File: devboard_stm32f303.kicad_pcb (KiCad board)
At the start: 2 copper layers, 50 x 17.8 mm, 22 parts, among them J1 Conn_01x04, J2 USB_B_Mini, J3 Conn_01x20, J4 Conn_01x20, SW1 SW_Push, U1 STM32F303CCTx, U2 AMS1117-3.3, Y1 Crystal_Small

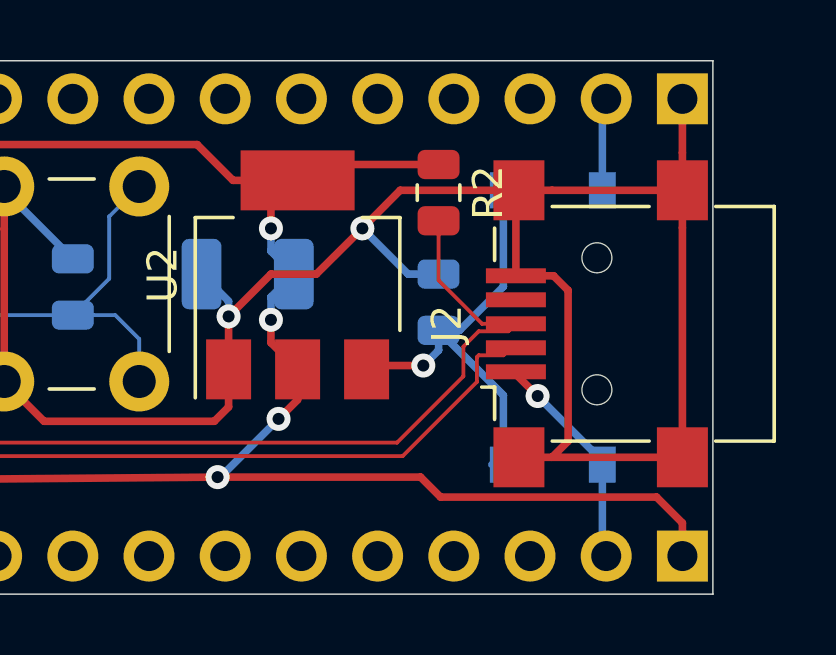
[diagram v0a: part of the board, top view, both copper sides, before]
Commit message: Add netlist tags
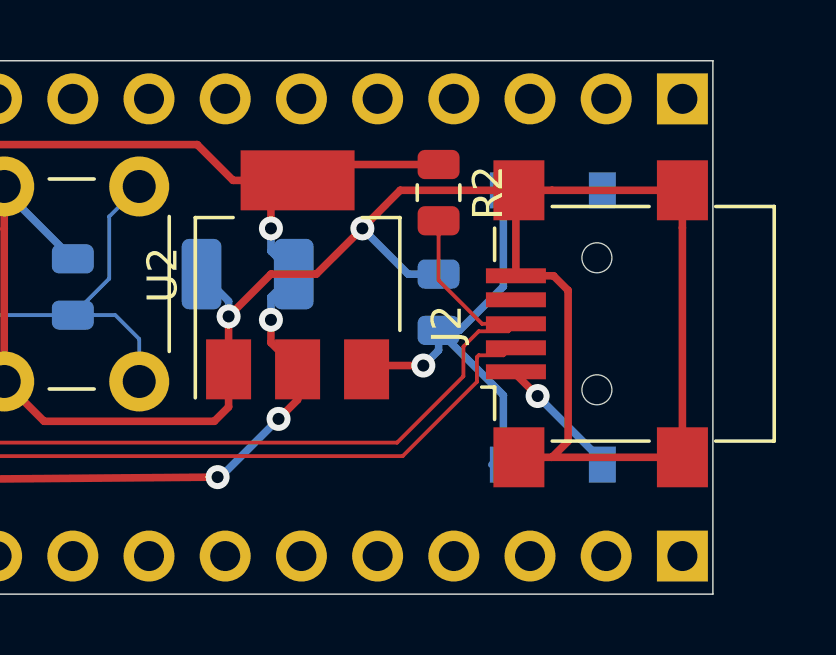
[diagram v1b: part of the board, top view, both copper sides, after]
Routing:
- net +3V3: track 125.7 -> 108.5 mm
- net GND: track 131.6 -> 128.6 mm
- net VBUS: track 7.39 -> 4.47 mm
- net VIN: track 2.85 -> 0.18 mm
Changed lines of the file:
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@@
     (thickness 1.6)
     (drawings 9)
-    (tracks 238)
+    (tracks 229)
     (zones 0)
     (modules 22)
@@
   (segment (start 125.589 30.875) (end 125.589 32.639) (width 0.254) (layer F.Cu) (net 1))
   (segment (start 127 29.464) (end 125.589 30.875) (width 0.254) (layer F.Cu) (net 1))
-  (segment (start 140.716 25.416) (end 140.716 23.622) (width 0.254) (layer F.Cu) (net 1))
-  (segment (start 140.716 26.67) (end 140.716 25.416) (width 0.254) (layer F.Cu) (net 1))
   (via (at 130.048 27.94) (size 0.8) (drill 0.4) (layers F.Cu B.Cu) (net 1))
   (segment (start 131.572 29.464) (end 130.048 27.94) (width 0.254) (layer B.Cu) (net 1))
@@
   (segment (start 101.91752 36.91402) (end 113.70798 36.91402) (width 0.254) (layer F.Cu) (net 4))
   (segment (start 128.016 26.466) (end 127.889 26.339) (width 0.254) (layer F.Cu) (net 4))
-  (segment (start 139.855001 36.897001) (end 132.655001 36.897001) (width 0.254) (layer F.Cu) (net 4))
-  (segment (start 140.716 37.758) (end 139.855001 36.897001) (width 0.254) (layer F.Cu) (net 4))
-  (segment (start 140.716 38.862) (end 140.716 37.758) (width 0.254) (layer F.Cu) (net 4))
-  (segment (start 131.989 36.231) (end 132.655001 36.897001) (width 0.254) (layer F.Cu) (net 4))
-  (segment (start 125.222 36.231) (end 131.989 36.231) (width 0.254) (layer F.Cu) (net 4))
   (segment (start 127.889 32.639) (end 127.889 31.877) (width 0.254) (layer F.Cu) (net 4))
   (segment (start 127.889 26.339) (end 127.889 27.051) (width 0.254) (layer F.Cu) (net 4))
@@
   (segment (start 103.886 28.448) (end 104.902 29.464) (width 0.127) (layer B.Cu) (net 12))
   (segment (start 138.048 23.75) (end 138.176 23.622) (width 0.254) (layer B.Cu) (net 81))
-  (segment (start 138.048 26.416) (end 138.048 23.75) (width 0.254) (layer B.Cu) (net 81))
   (segment (start 138.048 38.734) (end 138.176 38.862) (width 0.254) (layer B.Cu) (net 82))
-  (segment (start 138.048 35.814) (end 138.048 38.734) (width 0.254) (layer B.Cu) (net 82))
   (via (at 135.89 33.528) (size 0.8) (drill 0.4) (layers F.Cu B.Cu) (net 82))
   (segment (start 135.166 32.72) (end 135.166 32.804) (width 0.254) (layer F.Cu) (net 82))

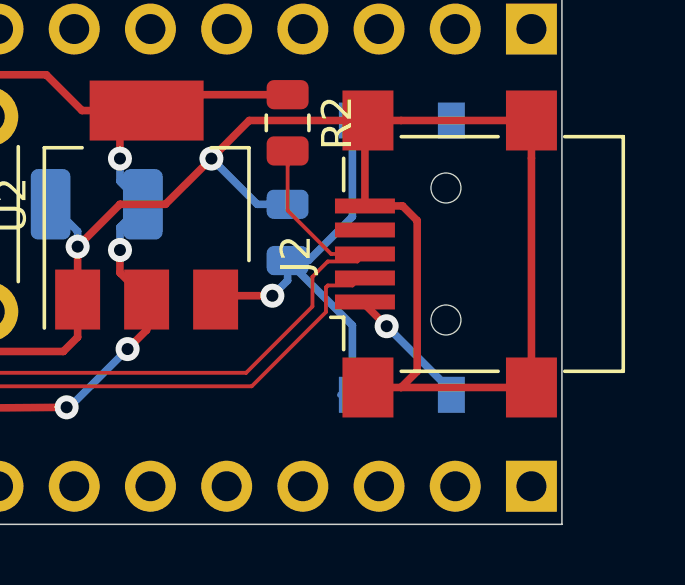
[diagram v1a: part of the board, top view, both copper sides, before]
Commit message: Add polyfuse
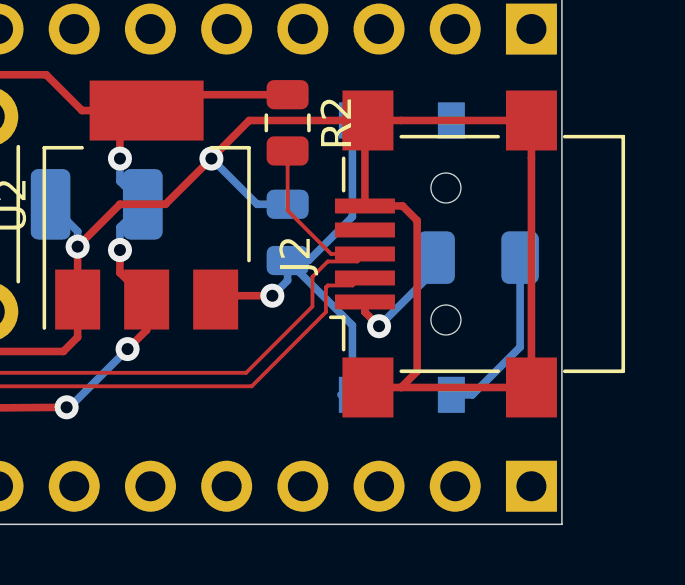
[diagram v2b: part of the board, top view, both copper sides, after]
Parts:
- added F1: Polyfuse_Small, Fuse:Fuse_1206_3216Metric, B.Cu at (138.9, 31.2)
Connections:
- net BOOT1 renamed PB2
- net Net-(U1-Pad10) renamed PA0
- net Net-(U1-Pad11) renamed PA1
- net Net-(U1-Pad12) renamed PA2
- net Net-(U1-Pad13) renamed PA3
- net Net-(U1-Pad14) renamed PA4
- net Net-(U1-Pad15) renamed PA5
- net Net-(U1-Pad16) renamed PA6
- net Net-(U1-Pad17) renamed PA7
- net Net-(U1-Pad18) renamed PB0
- net Net-(U1-Pad19) renamed PB1
- net Net-(U1-Pad21) renamed PB10
- net Net-(U1-Pad22) renamed PB11
- net Net-(U1-Pad25) renamed PB12
- net Net-(U1-Pad26) renamed PB13
- net Net-(U1-Pad27) renamed PB14
- net Net-(U1-Pad28) renamed PB15
- net Net-(U1-Pad29) renamed PA8
- net Net-(U1-Pad30) renamed PA9
- net Net-(U1-Pad31) renamed PA10
- net Net-(U1-Pad39) renamed PB3
- net Net-(U1-Pad40) renamed PB4
- net Net-(U1-Pad41) renamed PB5
- net Net-(U1-Pad42) renamed PB6
- net Net-(U1-Pad43) renamed PB7
- net Net-(U1-Pad45) renamed PB8
- net Net-(U1-Pad46) renamed PB9
- J2 pad 1: VBUS -> Net-(F1-Pad1)
- J3 pad 1: GND -> Net-(J3-Pad1)
- J3 pad 2: VIN -> Net-(J3-Pad2)
- J4 pad 1: +3V3 -> VBUS
- J4 pad 2: VBUS -> GND
- J4 pad 3: Net-(J4-Pad3) -> RESET
- J4 pad 4: Net-(J4-Pad4) -> +3V3
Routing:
- net Net-(F1-Pad1): track 0.00 -> 4.16 mm, vias 0 -> 1
- net VBUS: track 4.47 -> 6.06 mm, vias 1 -> 0

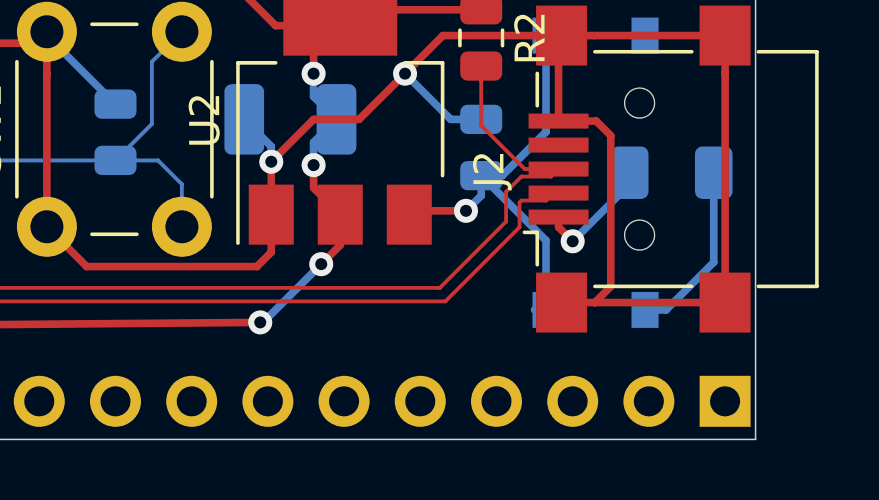
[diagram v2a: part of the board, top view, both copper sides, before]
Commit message: Power routing
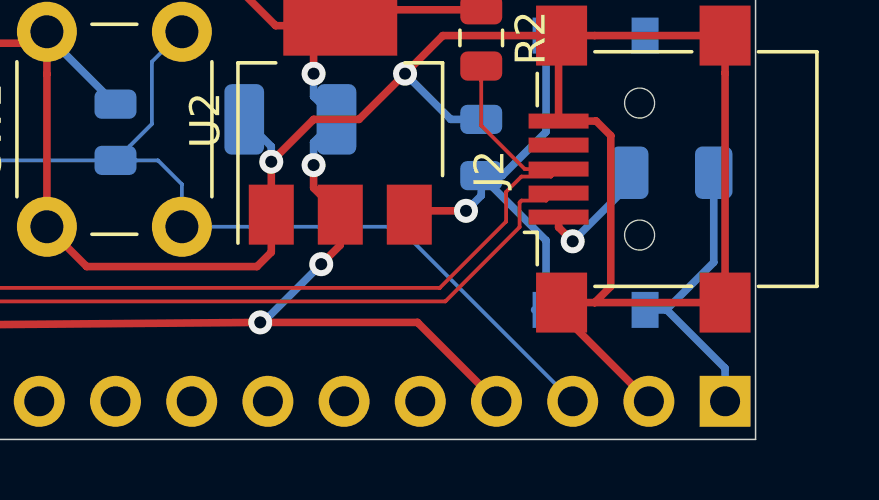
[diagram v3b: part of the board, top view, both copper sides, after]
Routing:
- net RESET: track 29.3 -> 44.8 mm
- net +3V3: track 108.5 -> 117.4 mm
- net GND: track 128.8 -> 133.3 mm
- net VBUS: track 6.06 -> 9.93 mm

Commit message: Start new routing
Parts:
- removed J1: Conn_01x04, Connector_PinHeader_2.54mm:PinHeader_1x04_P2.54mm_Vertical
- removed SW1: SW_Push, Button_Switch_THT:SW_PUSH_6mm
- C5: moved to B.Cu
- D1: moved to F.Cu
- JP1: footprint Connector_PinHeader_2.54mm:PinHeader_1x03_P2.54mm_Vertical -> Jumper:SolderJumper-3_P1.3mm_Open_Pad1.0x1.5mm
- moved JP1 30.3 mm to (84.6, 30.2), turned to 90 degrees
- moved R1 30.0 mm to (81.6, 30.5)
- moved C1 20.5 mm to (115.6, 33.4), turned to 90 degrees
- moved C2 20.2 mm to (115.6, 29.8), turned to 270 degrees
- moved Y1 16.4 mm to (112.6, 31.6), turned to 90 degrees
- moved D2 15.0 mm to (149.7, 33.5)
- moved C8 10.3 mm to (142.7, 31.9)
- moved F1 6.61 mm to (132.3, 31.1), turned to 270 degrees
- moved C6 5.42 mm to (120.1, 35.3), turned to 0 degrees
- moved D1 4.98 mm to (131.4, 35.3)
- moved C5 1.31 mm to (111.4, 36.1), turned to 180 degrees
- moved C3 1.25 mm to (111.4, 26.4)
- moved C7 1.15 mm to (98.5, 26.4), turned to 0 degrees
- moved C4 1.14 mm to (98.5, 36.1)
- moved U2 0.38 mm to (127.5, 29.5)
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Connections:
- net Net-(J3-Pad18) renamed PA15
- J3 pad 1: Net-(J3-Pad1) -> PA9
- J3 pad 10: Net-(J3-Pad10) -> PB2
- J3 pad 11: Net-(J3-Pad11) -> PB1
- J3 pad 12: Net-(J3-Pad12) -> PB0
- J3 pad 13: Net-(J3-Pad13) -> PA4
- J3 pad 14: Net-(J3-Pad14) -> PA5
- J3 pad 15: Net-(J3-Pad15) -> PA6
- J3 pad 16: Net-(J3-Pad16) -> PA7
- J3 pad 17: Net-(J3-Pad17) -> PA8
- J3 pad 2: Net-(J3-Pad2) -> PA10
- J3 pad 3: Net-(J3-Pad3) -> GND
- J3 pad 4: Net-(J3-Pad4) -> GND
- J3 pad 5: Net-(J3-Pad5) -> PB7
- J3 pad 6: Net-(J3-Pad6) -> PB6
- J3 pad 7: Net-(J3-Pad7) -> PB5
- J3 pad 8: Net-(J3-Pad8) -> PB4
- J3 pad 9: Net-(J3-Pad9) -> PB3
- J4 pad 10: Net-(J4-Pad10) -> PB14
- J4 pad 11: Net-(J4-Pad11) -> PB15
- J4 pad 12: Net-(J4-Pad12) -> PB9
- J4 pad 13: Net-(J4-Pad13) -> PB10
- J4 pad 14: Net-(J4-Pad14) -> PB11
- J4 pad 15: Net-(J4-Pad15) -> PB12
- J4 pad 16: Net-(J4-Pad16) -> SWCLK
- J4 pad 17: Net-(J4-Pad17) -> SWDIO
- J4 pad 18: Net-(J4-Pad18) -> RESET
- J4 pad 5: Net-(J4-Pad5) -> PA2
- J4 pad 6: Net-(J4-Pad6) -> PA1
- J4 pad 7: Net-(J4-Pad7) -> PA0
- J4 pad 8: Net-(J4-Pad8) -> PB8
- J4 pad 9: Net-(J4-Pad9) -> PB13
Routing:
- net GND: track 133.3 -> 36.5 mm
- net +3V3: track 117.4 -> 40.0 mm, vias 5 -> 3
- net RESET: track 44.8 -> 0.00 mm, vias 1 -> 0
- net SWCLK: track 18.5 -> 0.00 mm, vias 1 -> 0
- net SWDIO: track 16.8 -> 0.00 mm, vias 1 -> 0
- net Net-(C8-Pad1): track 15.1 -> 2.67 mm, vias 1 -> 0
- net BOOT0: track 8.63 -> 0.00 mm, vias 1 -> 0
- net VBUS: track 9.93 -> 3.11 mm, vias 0 -> 1
- net OSC_OUT: track 8.49 -> 12.8 mm
- net Net-(F1-Pad1): track 4.16 -> 8.07 mm
- net D-: track 32.4 -> 35.6 mm, vias 0 -> 2
- net OSC_IN: track 7.40 -> 9.87 mm
- net Net-(JP1-Pad2): track 2.16 -> 0.00 mm
- net D+: track 37.8 -> 37.1 mm, vias 0 -> 4

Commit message: More routing
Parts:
- removed D2: 1N5819, Diode_SMD:D_SOD-123
- C6, C8: moved to F.Cu
- moved C8 17.9 mm to (125.1, 35.1), turned to 180 degrees
- moved R1 13.9 mm to (95.5, 30.8), turned to 90 degrees
- moved C6 8.67 mm to (111.5, 36.1)
- moved JP1 8.52 mm to (93.1, 30.6)
- moved C9 1.27 mm to (127.5, 29.5)
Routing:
- net +3V3: track 40.0 -> 110.5 mm
- net BOOT0: track 0.00 -> 9.42 mm, vias 0 -> 3
- net GND: track 36.5 -> 45.2 mm
- net RESET: track 0.00 -> 6.81 mm, vias 0 -> 2
- net Net-(C8-Pad1): track 2.67 -> 6.68 mm
- net Net-(JP1-Pad2): track 0.00 -> 2.73 mm, vias 0 -> 1
